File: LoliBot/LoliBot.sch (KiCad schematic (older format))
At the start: 44 parts, among them J1 LOLINBATT, J10 LEFT-MOTOR, J11 REFLECT_, J12 MECH, J13 MECH, J14 MECH, J15 MECH, J16 MECH, J17 MECH, J18 MECH, J19 MECH, J2 APA106, J20 CONN_01X08, J21 CONN_01X08, J22 BRIDGE_RIGHT, J23 BRIDGE_LEFT, J24 FUSE_BRIDGE, J25 MECH, J26 MECH, J27 MECH, J28 MECH, J29 MECH, J3 SERVO1, J30 MECH, J31 LCA_LOGO, J32 FREETRONICS_LOGO, J4 RIGHT, J5 LEFT, J6 MPU-9250, J7 APA106, J8 APA106, J9 RIGHT-MOTOR, SW1 ON|OFF, U1 LOLIN32-LITE, U3 L9110, U4 L9110

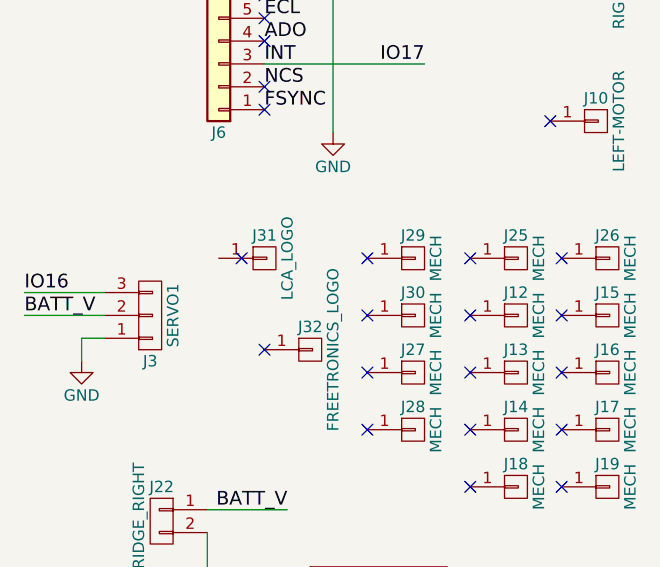
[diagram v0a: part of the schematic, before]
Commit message: fixed overhanging through holes.
Board production house didn't like vias that get cut in half
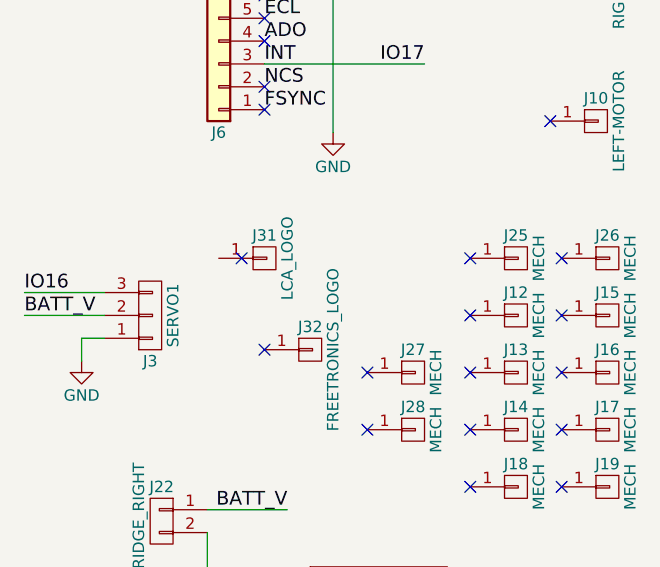
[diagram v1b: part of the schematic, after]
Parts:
- removed J29, J30: MECH, Mounting_Holes:MountingHole_3.2mm_M3_Pad, symbol CONN_01X01
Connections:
- no-connect marks 24 -> 22
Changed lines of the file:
@@
 NoConn ~ 9650 3400
-$Comp
-L CONN_01X01 J29
-U 1 1 5A295C52
-P 9850 2650
-F 0 "J29" H 9850 2750 50  0000 C CNN
-F 1 "MECH" V 9950 2650 50  0000 C CNN
-F 2 "Mounting_Holes:MountingHole_3.2mm_M3_Pad" H 9850 2650 50  0001 C CNN
-F 3 "" H 9850 2650 50  0001 C CNN
-	1    9850 2650
-	1    0    0    -1
-$EndComp
-$Comp
-L CONN_01X01 J30
-U 1 1 5A295C58
-P 9850 2900
-F 0 "J30" H 9850 3000 50  0000 C CNN
-F 1 "MECH" V 9950 2900 50  0000 C CNN
-F 2 "Mounting_Holes:MountingHole_3.2mm_M3_Pad" H 9850 2900 50  0001 C CNN
-F 3 "" H 9850 2900 50  0001 C CNN
-	1    9850 2900
-	1    0    0    -1
-$EndComp
-NoConn ~ 9650 2650
-NoConn ~ 9650 2900
 $Comp
 L CONN_01X01 J31
